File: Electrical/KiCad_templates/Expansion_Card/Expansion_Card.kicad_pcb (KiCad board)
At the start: 2 copper layers, 26 x 30 mm, 11 parts, among them P1 USB_C_Plug_USB2.0, U1 AP2112K-3.3

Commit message: Submitted for fabrication
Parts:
- removed C1, C2: 10uF, Capacitor_SMD:C_0805_2012Metric
- removed P1: USB_C_Plug_USB2.0, Expansion_Card:USB_C_Plug_Molex_105444
- removed R1: 5.1k, Resistor_SMD:R_0603_1608Metric
- removed TP1, TP2, TP3, TP4: TestPoint, TestPoint:TestPoint_Pad_1.5x1.5mm
- added USB1: TYPE-C 24P QT 143, easyeda2kicad:TYPE-C-SMD_C9900025773, F.Cu at (139.9, 150.4)
- U1: value AP2112K-3.3 -> U261-241N-4BC2SS; footprint Package_TO_SOT_SMD:SOT-23-5 -> easyeda2kicad:USB-C-SMD_XKB_U261-24XN-4BC2SS
- moved U1 11.8 mm to (140.0, 128.7), turned to 180 degrees
- moved H1 1.81 mm to (128.7, 144.7)
- moved H2 1.81 mm to (151.3, 144.7)
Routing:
- net VBUS: track 0.00 -> 43.3 mm
- net /USB_DN: track 0.00 -> 26.9 mm, vias 0 -> 2
- net /RX2+: track 0.00 -> 24.3 mm, vias 0 -> 2
- net /RX2-: track 0.00 -> 24.2 mm, vias 0 -> 2
- net /TX1+: track 0.00 -> 24.2 mm, vias 0 -> 2
- net /TX1-: track 0.00 -> 24.1 mm, vias 0 -> 2
- net /SBU1: track 0.00 -> 23.9 mm, vias 0 -> 2
- net /CC: track 0.00 -> 23.9 mm, vias 0 -> 2
- net /USB_DP: track 0.00 -> 21.7 mm
- net /Vconn: track 0.00 -> 18.2 mm
- net /RX1+: track 0.00 -> 18.2 mm
- net /RX1-: track 0.00 -> 18.2 mm
- net /TX2-: track 0.00 -> 18.2 mm
- net /TX2+: track 0.00 -> 18.2 mm
- net /SBU2: track 0.00 -> 18.2 mm
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- added copper zone on F.Cu, net GND
- added copper zone on In1.Cu, net GND
- added copper zone on In2.Cu, net GND
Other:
- board size 26 x 30 mm -> 26 x 28.2 mm
- copper layers 2 -> 4
- net class Default removed
- board text added: "USB-C Framework Module V1a Danny Hills 07/06/2026"

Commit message: Updated PCB and Re-Ordered
+ Added Local Libraries to Project
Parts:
- added REF**: KiCad-Logo2_5mm_SilkScreen, Symbol:KiCad-Logo2_5mm_SilkScreen, F.Cu at (148.1, 134.4)
- moved USB1 1.00 mm to (139.9, 149.4)
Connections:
- U1 pad A10: /TX2- -> /RX2-
- U1 pad A11: /TX2+ -> /RX2+
- U1 pad A2: /RX1+ -> /TX1+
- U1 pad A3: /RX1- -> /TX1-
- U1 pad A5: /SBU2 -> /CC1
- U1 pad A8: /Vconn -> /SBU1
- U1 pad B10: /TX1- -> /RX1-
- U1 pad B11: /TX1+ -> /RX1+
- U1 pad B2: /RX2+ -> /TX2+
- U1 pad B3: /RX2- -> /TX2-
- U1 pad B5: /SBU1 -> /CC2
- U1 pad B6: /USB_DN -> /USB_DP
- U1 pad B7: /USB_DP -> /USB_DN
- U1 pad B8: /CC -> /SBU2
- USB1 pad A10: /TX2- -> /RX2-
- USB1 pad A11: /TX2+ -> /RX2+
- USB1 pad A2: /RX1+ -> /TX1+
- USB1 pad A3: /RX1- -> /TX1-
- USB1 pad A5: /SBU2 -> /CC1
- USB1 pad A8: /Vconn -> /SBU1
- USB1 pad B10: /TX1- -> /RX1-
- USB1 pad B11: /TX1+ -> /RX1+
- USB1 pad B2: /RX2+ -> /TX2+
- USB1 pad B3: /RX2- -> /TX2-
- USB1 pad B5: /SBU1 -> /CC2
- USB1 pad B8: /CC -> /SBU2
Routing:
- net /CC: track 23.9 -> 0.00 mm, vias 2 -> 0
- net /CC2: track 0.00 -> 22.9 mm, vias 0 -> 2
- net /Vconn: track 18.2 -> 0.00 mm
- net /CC1: track 0.00 -> 17.2 mm
- net /RX2+: track 24.3 -> 17.2 mm, vias 2 -> 0
- net /RX2-: track 24.2 -> 17.2 mm, vias 2 -> 0
- net /TX1+: track 24.2 -> 17.2 mm, vias 2 -> 0
- net /TX1-: track 24.1 -> 17.2 mm, vias 2 -> 0
- net /SBU1: track 23.9 -> 17.2 mm, vias 2 -> 0
- net /TX2+: track 18.2 -> 23.3 mm, vias 0 -> 2
- net /TX2-: track 18.2 -> 23.2 mm, vias 0 -> 2
- net /RX1+: track 18.2 -> 23.2 mm, vias 0 -> 2
- net /RX1-: track 18.2 -> 23.1 mm, vias 0 -> 2
- net /SBU2: track 18.2 -> 22.9 mm, vias 0 -> 2
- net /USB_DN: track 26.9 -> 22.3 mm
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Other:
- board size 26 x 28.2 mm -> 26 x 26.3 mm
- board text added: "USB-C Framework Module V1b Danny Hills 17/06/2026"
- board text removed: "USB-C Framework Module V1a Danny Hills 07/06/2026"

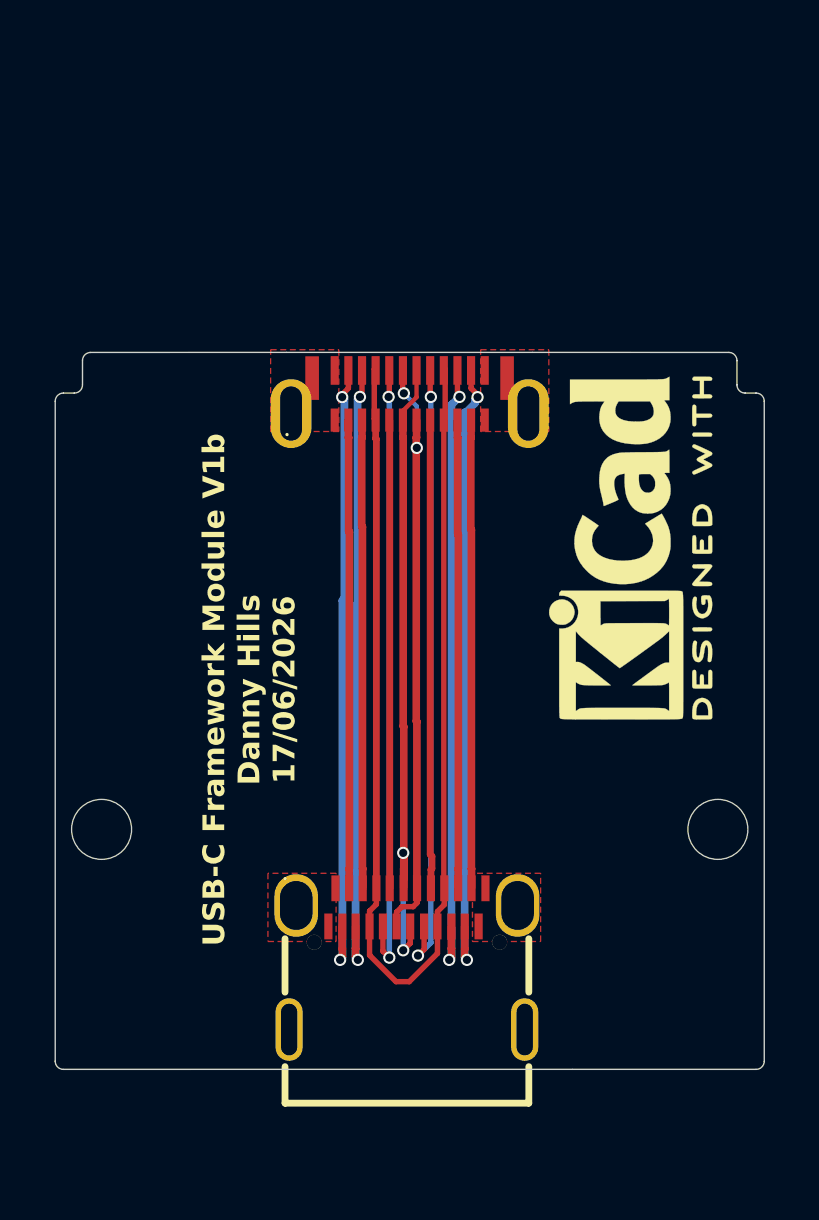
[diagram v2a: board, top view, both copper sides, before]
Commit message: Updated to use local footprint library
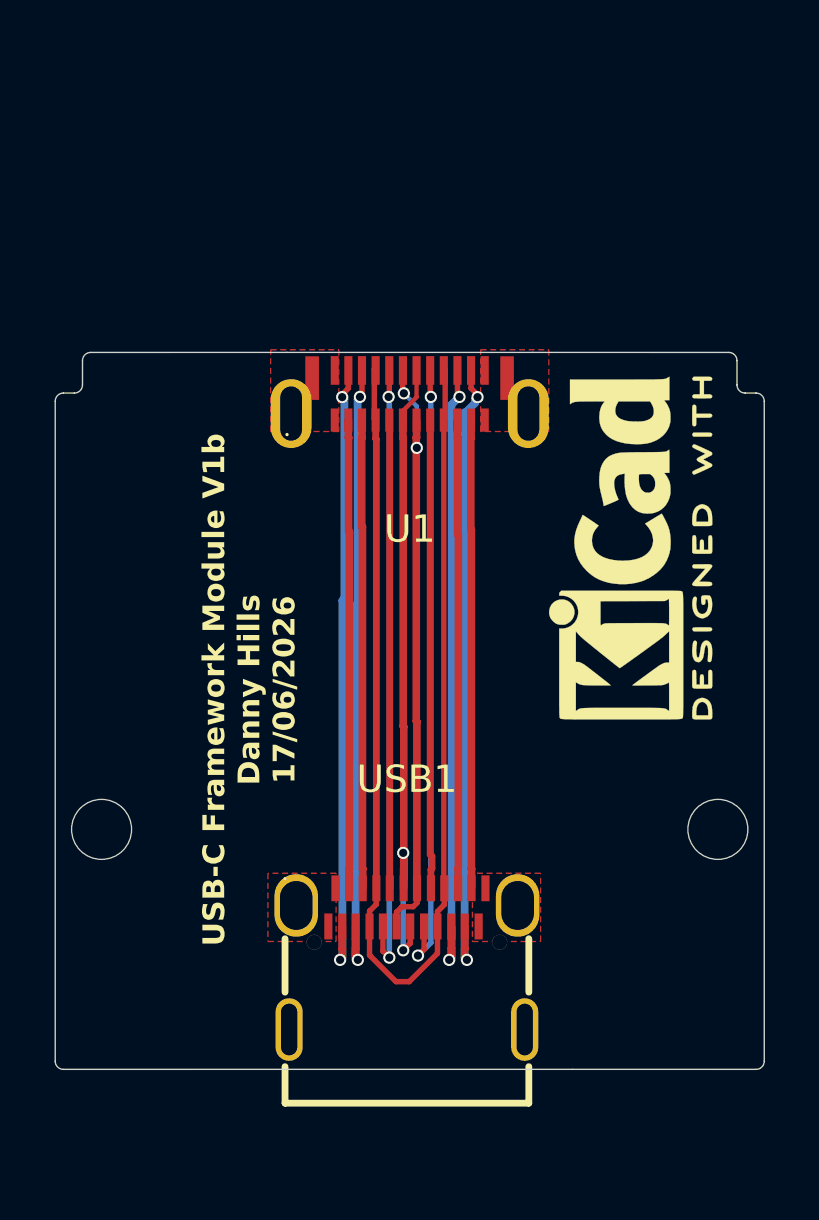
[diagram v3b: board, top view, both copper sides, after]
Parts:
- U1: footprint easyeda2kicad:USB-C-SMD_XKB_U261-24XN-4BC2SS -> project_library:USB-C-SMD_XKB_U261-24XN-4BC2SS
- USB1: footprint easyeda2kicad:TYPE-C-SMD_C9900025773 -> project_library:TYPE-C-SMD_C9900025773
